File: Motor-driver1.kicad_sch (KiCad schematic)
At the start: 32 parts, among them J8 PINHD_1x4_Male, J9 PINHD_1x4_Male, U2 DRV8825PWP, U3 DRV8825PWP

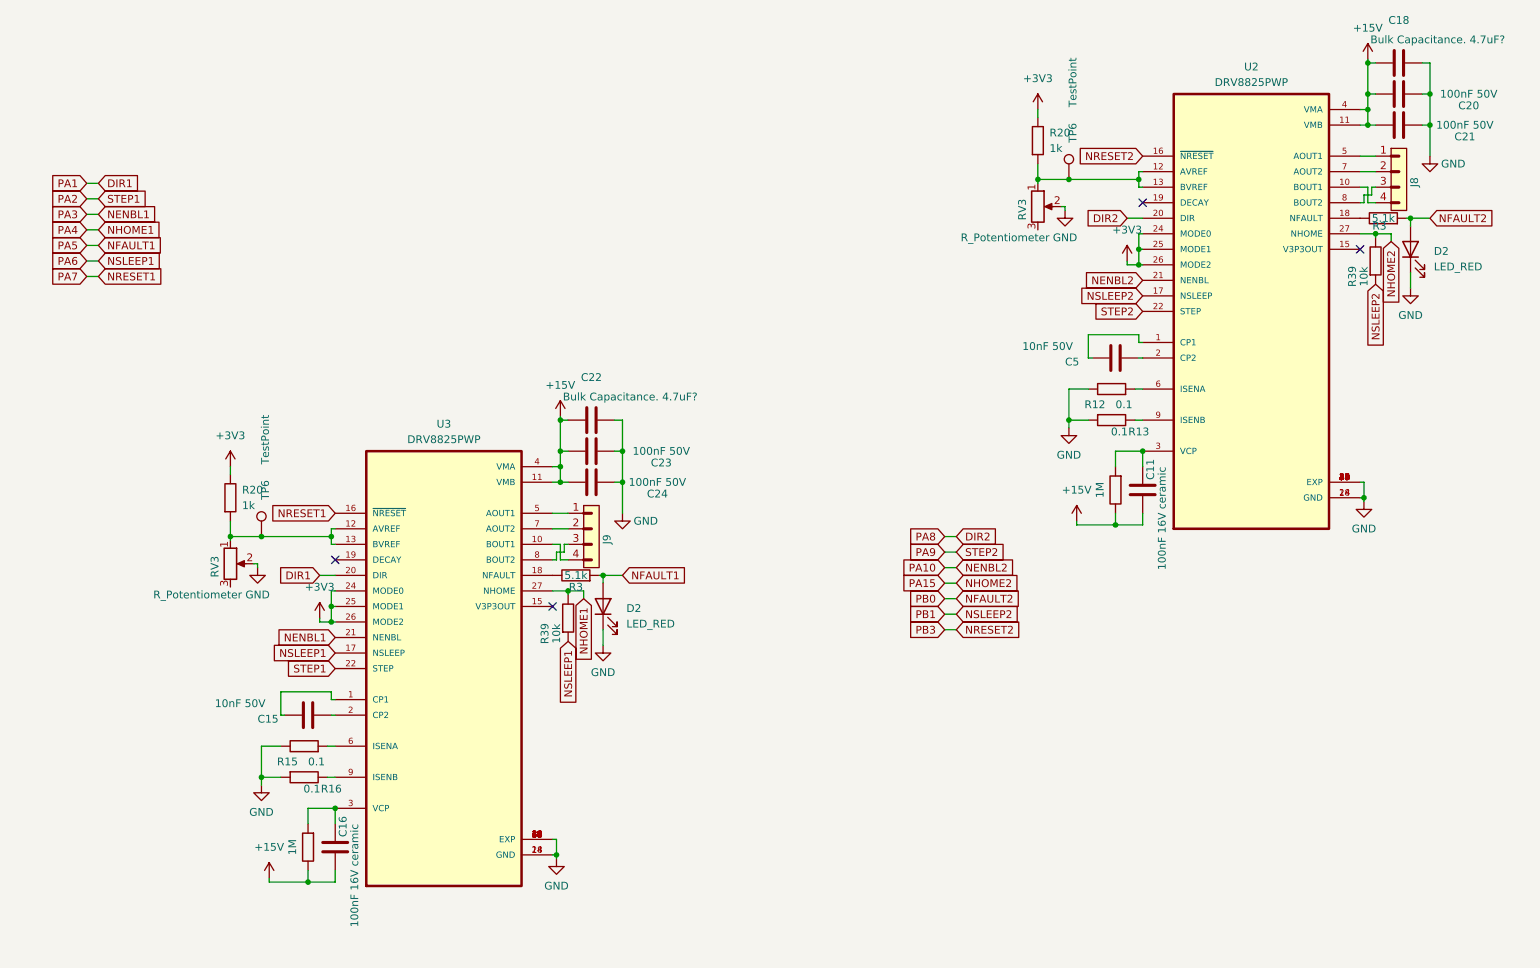
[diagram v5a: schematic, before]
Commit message: finished PCB. DRC 0 errors
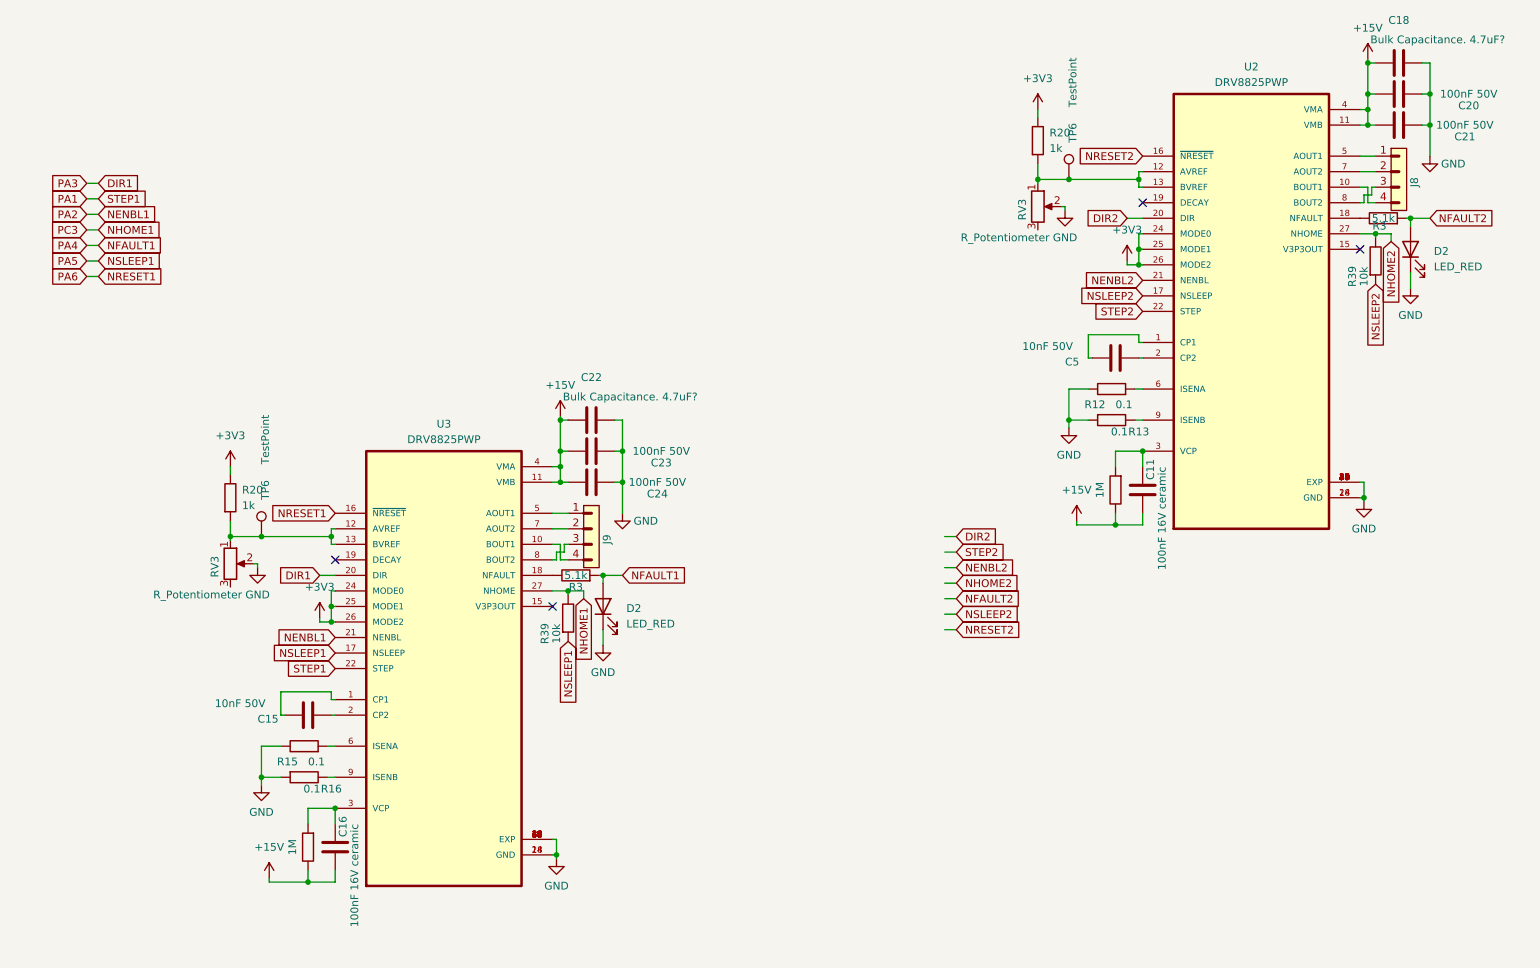
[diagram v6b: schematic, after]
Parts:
- TP6: footprint TestPoint:TestPoint_Pad_D2.5mm -> TestPoint:TestPoint_Pad_D1.5mm
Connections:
- net PA2 renamed PA1
- net PA9 renamed STEP2

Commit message: last polishing on pcb v1. ich isch abgabe dc
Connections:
- net STEP2 renamed PC4
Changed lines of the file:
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@@
+    )
+  )
+  (global_label "PA7" (shape input) (at 186.69 119.38 180) (fields_autoplaced)
+    (effects (font (size 1.27 1.27)) (justify right))
+    (property "Intersheetrefs" "${INTERSHEET_REFS}" (at 180.1367 119.38 0)
+      (effects (font (size 1.27 1.27)) (justify right) hide)
     )
   )
@@
     )
   )
+  (global_label "PC4" (shape input) (at 186.69 114.3 180) (fields_autoplaced)
+    (effects (font (size 1.27 1.27)) (justify right))
+    (property "Intersheetrefs" "${INTERSHEET_REFS}" (at 179.9553 114.3 0)
+      (effects (font (size 1.27 1.27)) (justify right) hide)
+    )
+  )
   (global_label "NSLEEP2" (shape input) (at 219.075 72.39 180) (fields_autoplaced)
     (effects (font (size 1.27 1.27)) (justify right))
@@
     )
   )
+  (global_label "PB10" (shape input) (at 186.69 124.46 180) (fields_autoplaced)
+    (effects (font (size 1.27 1.27)) (justify right))
+    (property "Intersheetrefs" "${INTERSHEET_REFS}" (at 178.7458 124.46 0)
+      (effects (font (size 1.27 1.27)) (justify right) hide)
+    )
+  )
   (global_label "PC3" (shape input) (at 46.355 61.595 180) (fields_autoplaced)
     (effects (font (size 1.27 1.27)) (justify right))
@@
     )
   )
+  (global_label "PB0" (shape input) (at 186.69 116.84 180) (fields_autoplaced)
+    (effects (font (size 1.27 1.27)) (justify right))
+    (property "Intersheetrefs" "${INTERSHEET_REFS}" (at 179.9553 116.84 0)
+      (effects (font (size 1.27 1.27)) (justify right) hide)
+    )
+  )
+  (global_label "PB1" (shape input) (at 186.69 121.92 180) (fields_autoplaced)
+    (effects (font (size 1.27 1.27)) (justify right))
+    (property "Intersheetrefs" "${INTERSHEET_REFS}" (at 179.9553 121.92 0)
+      (effects (font (size 1.27 1.27)) (justify right) hide)
+    )
+  )
   (global_label "NSLEEP1" (shape input) (at 125.095 128.905 270) (fields_autoplaced)
     (effects (font (size 1.27 1.27)) (justify right))
@@
     )
   )
+  (global_label "PC5" (shape input) (at 186.69 111.76 180) (fields_autoplaced)
+    (effects (font (size 1.27 1.27)) (justify right))
+    (property "Intersheetrefs" "${INTERSHEET_REFS}" (at 179.9553 111.76 0)
+      (effects (font (size 1.27 1.27)) (justify right) hide)
+    )
+  )
   (global_label "NSLEEP1" (shape input) (at 48.26 66.675 0) (fields_autoplaced)
     (effects (font (size 1.27 1.27)) (justify left))
@@
       (effects (font (size 1.27 1.27)) (justify right) hide)
     )
+  )
+  (global_label "PA10" (shape input) (at 186.69 127 180) (fields_autoplaced)
+    (effects (font (size 1.27 1.27)) (justify right))
+    (property "Intersheetrefs" "${INTERSHEET_REFS}" (at 178.9272 127 0)
+      (effects (font (size 1.27 1.27)) (justify right) hide)
+    )

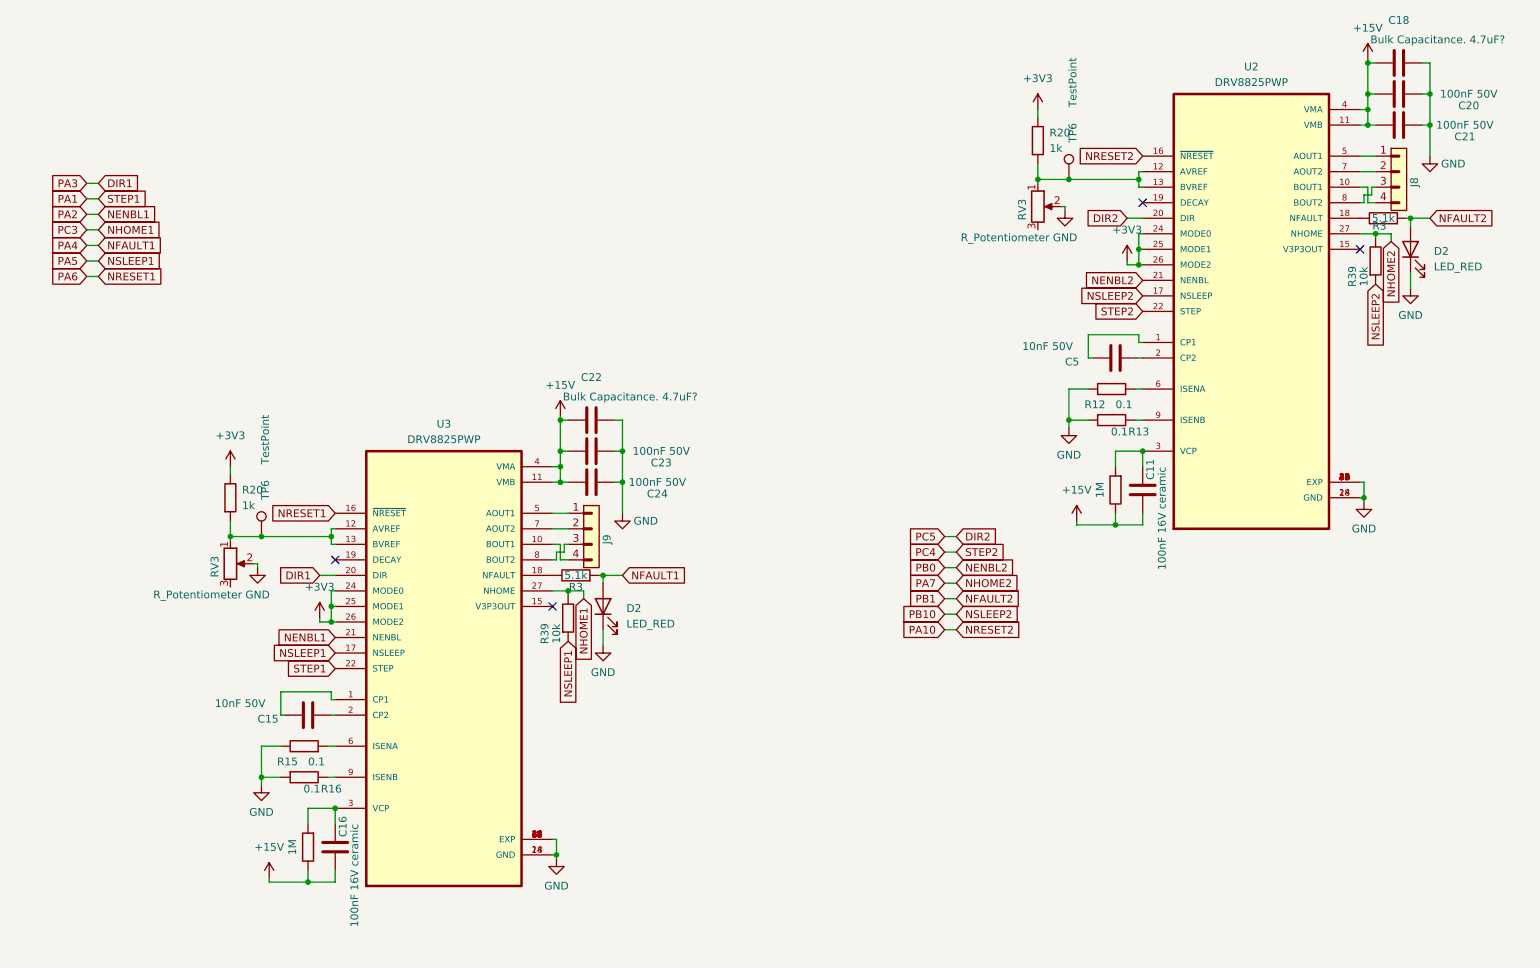
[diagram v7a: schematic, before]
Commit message: completly reroutet EVERYTHING
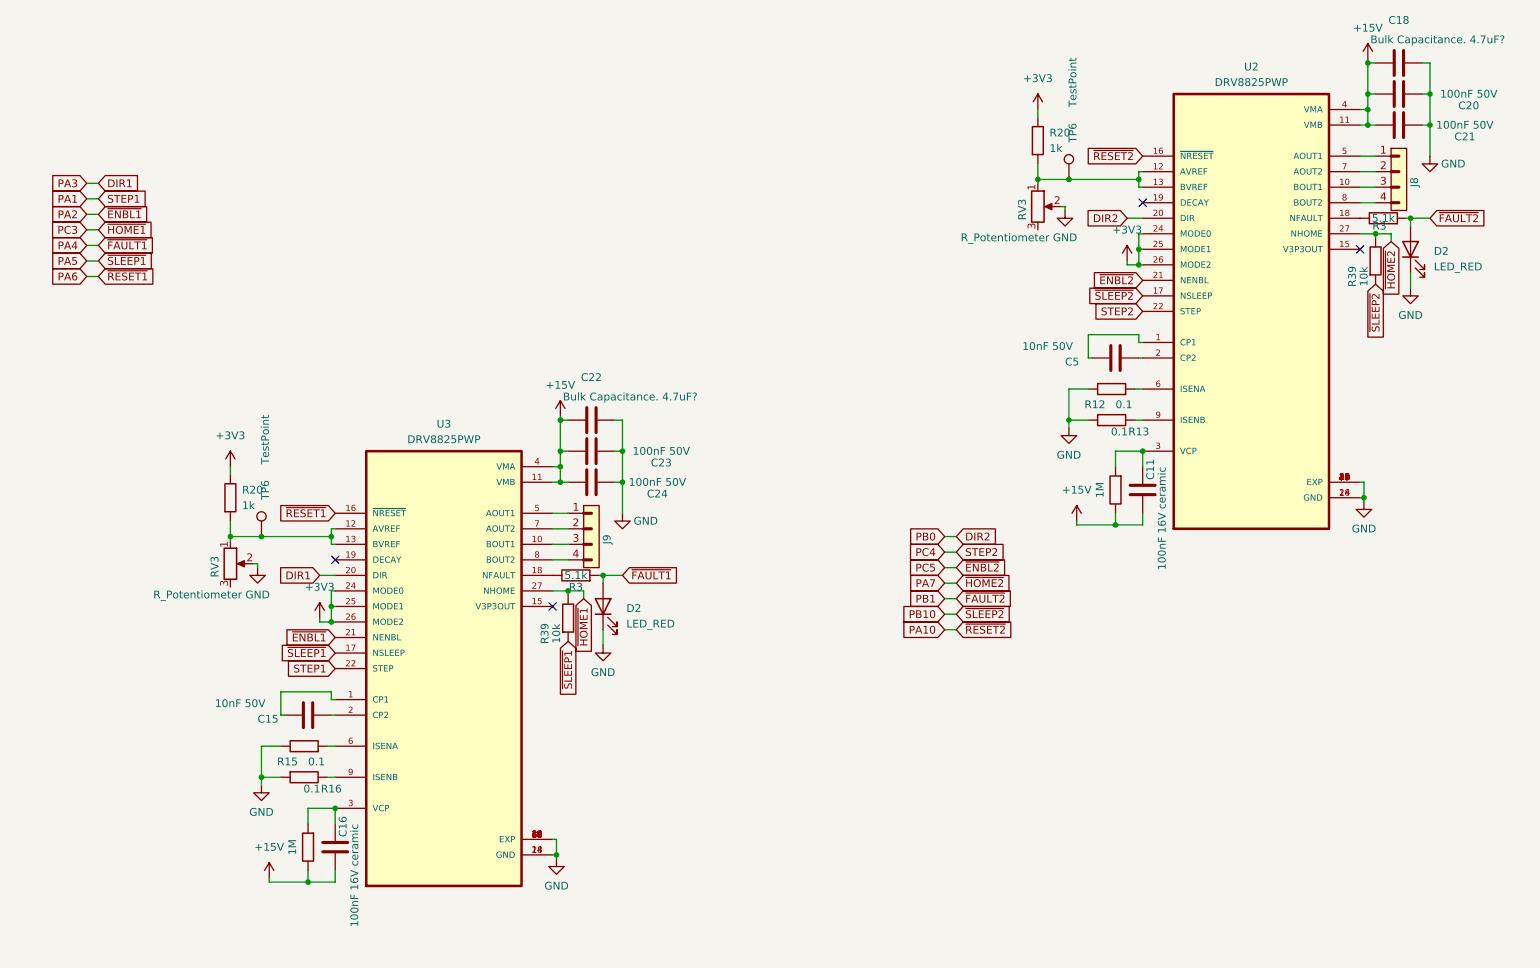
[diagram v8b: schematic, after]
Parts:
- RV3: footprint Potentiometer_THT:Potentiometer_ACP_CA6-H2,5_Horizontal -> poti:3386P1473LF
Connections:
- net at J9.3: now also U3.10 (BOUT1); no longer U3.8 (BOUT2)
- net at J9.4: now also U3.8 (BOUT2); no longer U3.10 (BOUT1)
- net at U2.10 (BOUT1): now also J8.3; no longer J8.4
- net at U2.8 (BOUT2): now also J8.4; no longer J8.3
- net NENBL1 renamed PA2
- net NENBL2 renamed PC5
- net NFAULT1 renamed PA4
- net NFAULT2 renamed PB1
- net NHOME1 renamed PC3
- net NHOME2 renamed PA7
- net NRESET1 renamed PA6
- net NRESET2 renamed PA10
- net NSLEEP1 renamed PA5
- net NSLEEP2 renamed PB10
